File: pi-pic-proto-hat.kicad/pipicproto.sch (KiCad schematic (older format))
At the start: 20 parts, among them J1 RUN/~PGM~, J10 Conn_01x13_Male, J22 Conn_01x13_Male, J6 Barrel_Jack_Switch, J7 Conn_01x24_Male, J8 Conn_01x06_Male, J9 Conn_01x02_Male, P1 Conn_02x20_Odd_Even, Q1 IRF4905, U1 PIC12F675-IP

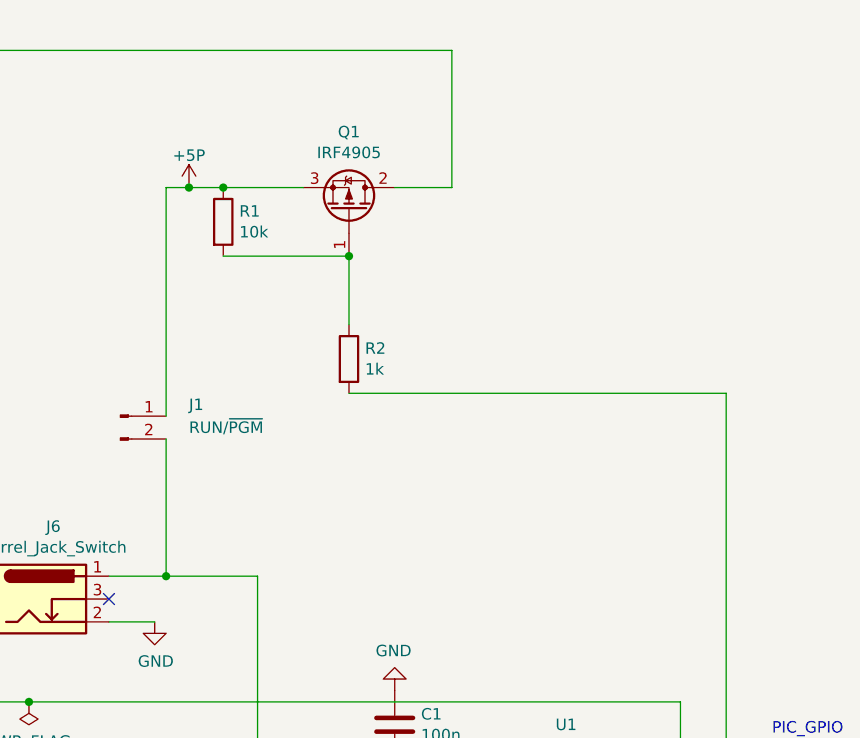
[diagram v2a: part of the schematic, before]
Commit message: V2.11: added LEDs
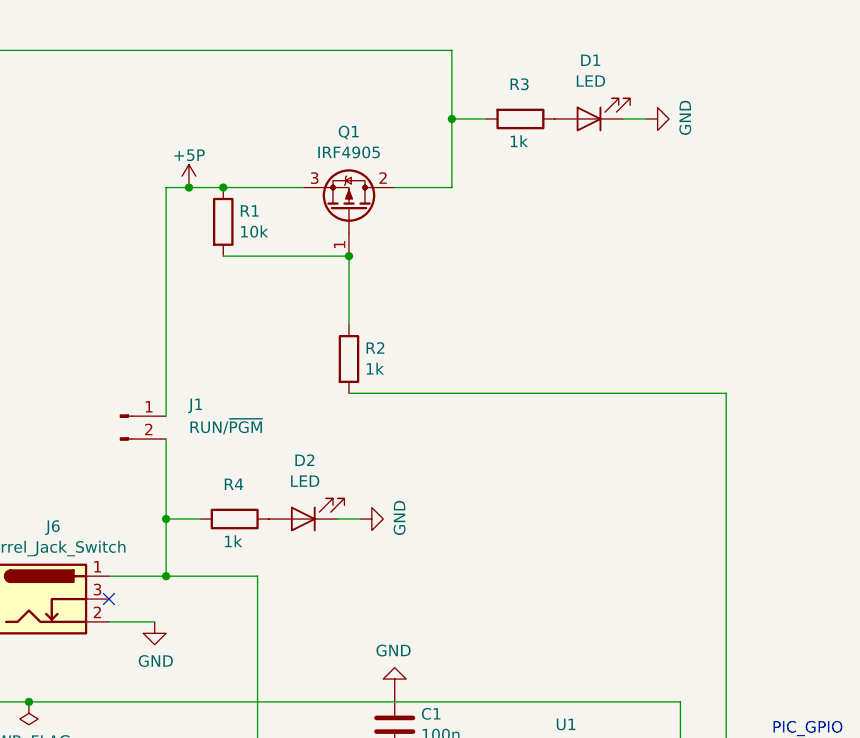
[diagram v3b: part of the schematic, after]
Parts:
- added D1, D2: LED, LED_SMD:LED_1206_3216Metric_Pad1.42x1.75mm_HandSolder, symbol Device:LED
- added R3, R4: 1k, Resistor_SMD:R_1206_3216Metric_Pad1.42x1.75mm_HandSolder, symbol Device:R
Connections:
- net +5V: now also R3.2
- net +5VP: now also R4.2
- net GND: now also D1.1 (K), D2.1 (K)
- new net: D1.2 (A), R3.1
- new net: D2.2 (A), R4.1
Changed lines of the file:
@@
 Sheet 1 1
 Title "PI PIC Prototyping Area"
-Date "2020-07-03"
-Rev "2.10"
+Date "2020-07-18"
+Rev "2.11"
 Comp "Bernhard Bablok, Lothar Hiller"
 Comment1 "https://github.com/bablokb/pi-pic-proto-hat"
@@
 Wire Wire Line
 	7500 1500 7750 1500
-Wire Wire Line
-	7750 900  7750 1500
 $Comp
 L Connector:Conn_01x13_Male J22
@@
 	6500 1500 6500 2500
 Wire Wire Line
-	6500 2600 6500 3200
+	6500 2600 6500 2950
 Connection ~ 6500 3200
 Wire Wire Line
@@
 Wire Wire Line
 	6900 3200 6900 4300
+$Comp
+L Device:R R3
+U 1 1 5F130E6C
+P 8050 1200
+F 0 "R3" V 7900 1150 50  0000 L CNN
+F 1 "1k" V 8150 1150 50  0000 L CNN
+F 2 "Resistor_SMD:R_1206_3216Metric_Pad1.42x1.75mm_HandSolder" V 7980 1200 50  0001 C CNN
+F 3 "~" H 8050 1200 50  0001 C CNN
+	1    8050 1200
+	0    1    1    0
+$EndComp
+$Comp
+L Device:LED D1
+U 1 1 5F137581
+P 8350 1200
+F 0 "D1" H 8343 945 50  0000 C CNN
+F 1 "LED" H 8343 1036 50  0000 C CNN
+F 2 "LED_SMD:LED_1206_3216Metric_Pad1.42x1.75mm_HandSolder" H 8350 1200 50  0001 C CNN
+F 3 "~" H 8350 1200 50  0001 C CNN
+	1    8350 1200
+	-1   0    0    1
+$EndComp
+$Comp
+L power:GND #PWR03
+U 1 1 5F14E188
+P 8600 1200
+F 0 "#PWR03" H 8600 950 50  0001 C CNN
+F 1 "GND" H 8605 1027 50  0000 C CNN
+F 2 "" H 8600 1200 50  0001 C CNN
+F 3 "" H 8600 1200 50  0001 C CNN
+	1    8600 1200
+	0    -1   -1   0
+$EndComp
+Wire Wire Line
+	7750 900  7750 1200
+Wire Wire Line
+	8500 1200 8600 1200
+Wire Wire Line
+	7900 1200 7750 1200
+Connection ~ 7750 1200
+Wire Wire Line
+	7750 1200 7750 1500
+$Comp
+L Device:R R4
+U 1 1 5F16FFEA
+P 6800 2950
+F 0 "R4" V 6650 2900 50  0000 L CNN
+F 1 "1k" V 6900 2900 50  0000 L CNN
+F 2 "Resistor_SMD:R_1206_3216Metric_Pad1.42x1.75mm_HandSolder" V 6730 2950 50  0001 C CNN
+F 3 "~" H 6800 2950 50  0001 C CNN
+	1    6800 2950
+	0    1    1    0
+$EndComp
+$Comp
+L Device:LED D2
+U 1 1 5F16FFF0
+P 7100 2950
+F 0 "D2" H 7093 2695 50  0000 C CNN
+F 1 "LED" H 7093 2786 50  0000 C CNN
+F 2 "LED_SMD:LED_1206_3216Metric_Pad1.42x1.75mm_HandSolder" H 7100 2950 50  0001 C CNN
+F 3 "~" H 7100 2950 50  0001 C CNN
+	1    7100 2950
+	-1   0    0    1
+$EndComp
+$Comp
+L power:GND #PWR04
+U 1 1 5F16FFF6
+P 7350 2950
+F 0 "#PWR04" H 7350 2700 50  0001 C CNN
+F 1 "GND" H 7355 2777 50  0000 C CNN
+F 2 "" H 7350 2950 50  0001 C CNN
+F 3 "" H 7350 2950 50  0001 C CNN
+	1    7350 2950
+	0    -1   -1   0
+$EndComp
+Wire Wire Line
+	7250 2950 7350 2950
+Wire Wire Line
+	6650 2950 6500 2950
+Connection ~ 6500 2950
+Wire Wire Line
+	6500 2950 6500 3200
 $EndSCHEMATC

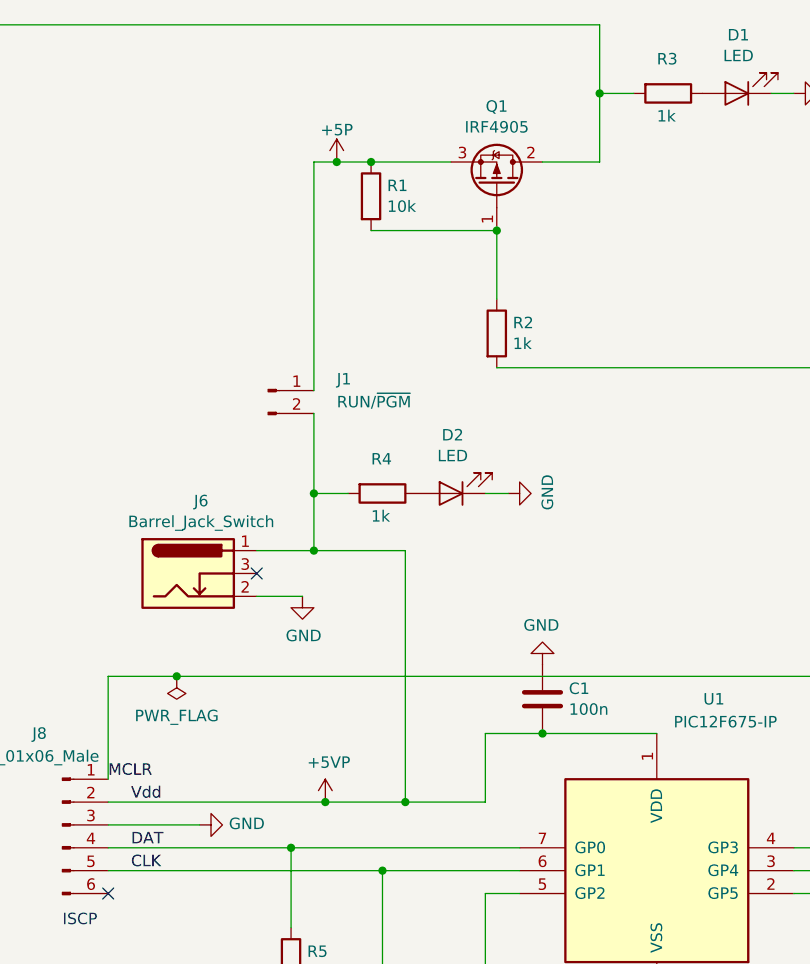
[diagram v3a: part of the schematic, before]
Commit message: V2.12: changed position of RUN-jumper
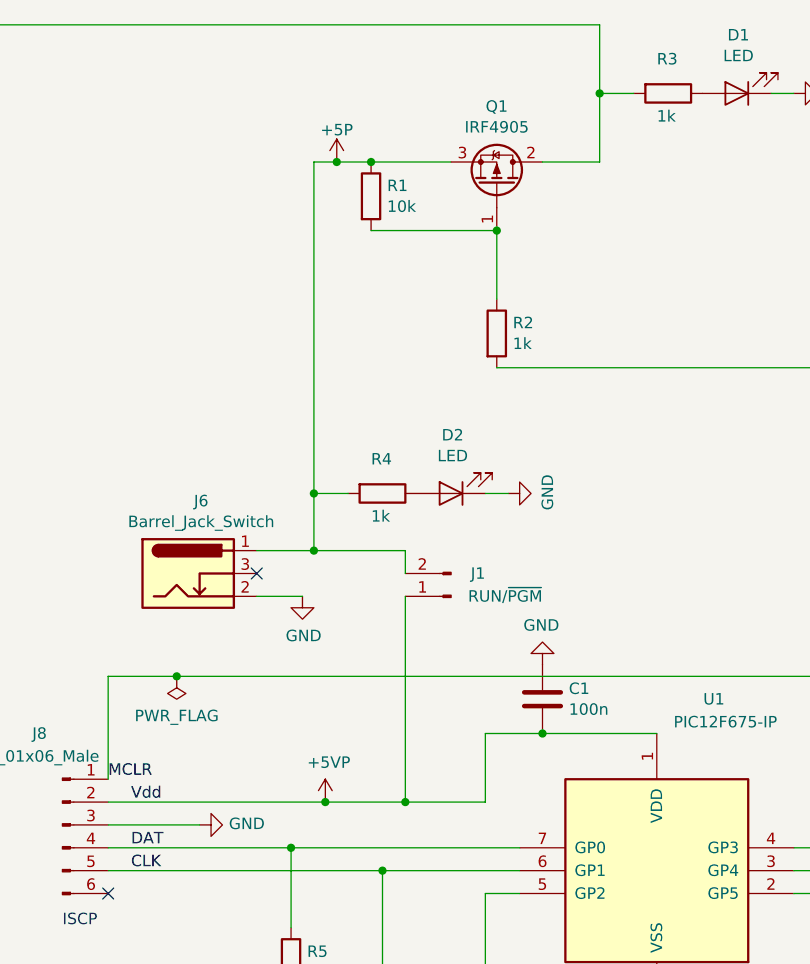
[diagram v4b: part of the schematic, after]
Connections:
- net +5P: now also J1.2 (Pin_2), J6.1, R4.2; no longer J1.1 (Pin_1)
- net +5VP: now also J1.1 (Pin_1); no longer J1.2 (Pin_2), J6.1, R4.2
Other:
- moved on the sheet: J1
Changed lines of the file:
@@
 Title "PI PIC Prototyping Area"
 Date "2020-07-18"
-Rev "2.11"
+Rev "2.12"
 Comp "Bernhard Bablok, Lothar Hiller"
 Comment1 "https://github.com/bablokb/pi-pic-proto-hat"
@@
 	1    0    0    -1
 $EndComp
-$Comp
-L Connector:Conn_01x02_Male J1
-U 1 1 5E41F5B6
-P 6300 2500
-F 0 "J1" H 6600 2550 50  0000 L CNN
-F 1 "RUN/~PGM~" H 6600 2450 50  0000 L CNN
-F 2 "Connector_PinHeader_2.54mm:PinHeader_1x02_P2.54mm_Vertical" H 6300 2500 50  0001 C CNN
-F 3 "~" H 6300 2500 50  0001 C CNN
-	1    6300 2500
-	1    0    0    -1
-$EndComp
 Wire Wire Line
 	3250 900  3250 1100
@@
 Wire Wire Line
 	6250 3200 6500 3200
-Wire Wire Line
-	6500 1500 6500 2500
-Wire Wire Line
-	6500 2600 6500 2950
 Connection ~ 6500 3200
-Wire Wire Line
-	6500 3200 6900 3200
 Wire Wire Line
 	6550 4300 6900 4300
@@
 	6900 4300 7250 4300
 Connection ~ 6900 4300
-Wire Wire Line
-	6900 3200 6900 4300
 $Comp
 L Device:R R3
@@
 Wire Wire Line
 	6500 2950 6500 3200
+$Comp
+L Connector:Conn_01x02_Male J1
+U 1 1 5E41F5B6
+P 7100 3400
+F 0 "J1" H 6950 3300 50  0000 L CNN
+F 1 "RUN/~PGM~" H 6700 3400 50  0000 L CNN
+F 2 "Connector_PinHeader_2.54mm:PinHeader_1x02_P2.54mm_Vertical" H 7100 3400 50  0001 C CNN
+F 3 "~" H 7100 3400 50  0001 C CNN
+	1    7100 3400
+	-1   0    0    1
+$EndComp
+Wire Wire Line
+	6900 3200 6900 3300
+Wire Wire Line
+	6900 3400 6900 4300
+Wire Wire Line
+	6500 1500 6500 2950
+Wire Wire Line
+	6500 3200 6900 3200
 $EndSCHEMATC

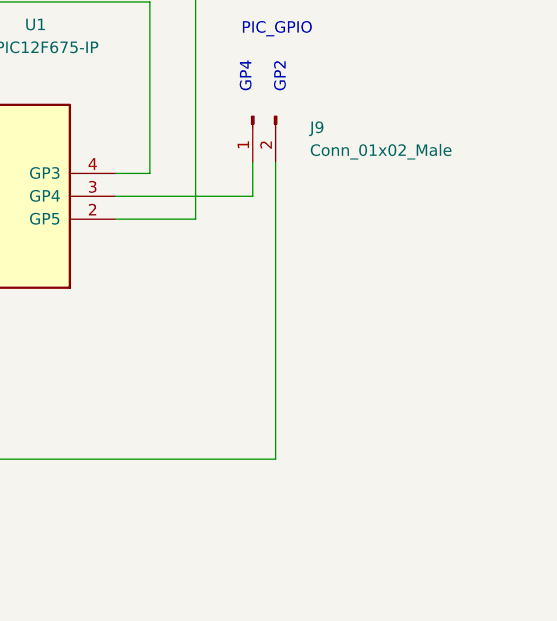
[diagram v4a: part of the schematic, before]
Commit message: V2.13: added button connected to GP2
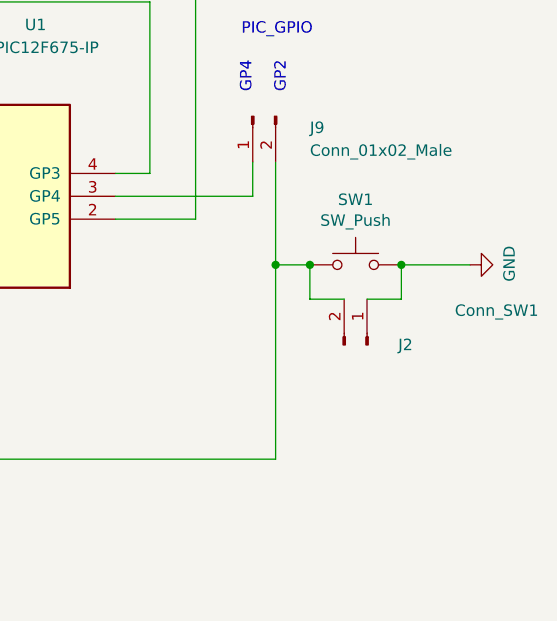
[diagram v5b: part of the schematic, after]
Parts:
- added J2: Conn_SW1, Connector_PinHeader_2.54mm:PinHeader_1x02_P2.54mm_Vertical, symbol Connector:Conn_01x02_Male
- added SW1: SW_Push, user:SW_PUSH_SLIM_1x4, symbol Switch:SW_Push
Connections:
- net GND: now also J2.1 (Pin_1), SW1.2
- net at J9.2 (Pin_2), U1.5 (GP2): now also J2.2 (Pin_2), SW1.1
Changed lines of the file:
@@
 Sheet 1 1
 Title "PI PIC Prototyping Area"
-Date "2020-07-18"
-Rev "2.12"
+Date "2020-07-23"
+Rev "2.13"
 Comp "Bernhard Bablok, Lothar Hiller"
 Comment1 "https://github.com/bablokb/pi-pic-proto-hat"
@@
 	7250 5750 9300 5750
 Wire Wire Line
-	9300 5750 9300 4450
+	9300 5750 9300 4900
 Text Notes 9200 4150 1    50   ~ 0
 GP4
@@
 Wire Wire Line
 	6500 3200 6900 3200
+$Comp
+L Switch:SW_Push SW1
+U 1 1 5F19E2FA
+P 9650 4900
+F 0 "SW1" H 9650 5185 50  0000 C CNN
+F 1 "SW_Push" H 9650 5094 50  0000 C CNN
+F 2 "user:SW_PUSH_SLIM_1x4" H 9650 5100 50  0001 C CNN
+F 3 "~" H 9650 5100 50  0001 C CNN
+	1    9650 4900
+	1    0    0    -1
+$EndComp
+Wire Wire Line
+	9450 4900 9300 4900
+Connection ~ 9300 4900
+Wire Wire Line
+	9300 4900 9300 4450
+$Comp
+L power:GND #PWR05
+U 1 1 5F1A4F9E
+P 10150 4900
+F 0 "#PWR05" H 10150 4650 50  0001 C CNN
+F 1 "GND" H 10155 4727 50  0000 C CNN
+F 2 "" H 10150 4900 50  0001 C CNN
+F 3 "" H 10150 4900 50  0001 C CNN
+	1    10150 4900
+	0    -1   -1   0
+$EndComp
+Wire Wire Line
+	9850 4900 10150 4900
+$Comp
+L Connector:Conn_01x02_Male J2
+U 1 1 5F1ABA22
+P 9700 5250
+F 0 "J2" V 9700 5450 50  0000 R CNN
+F 1 "Conn_SW1" V 9850 6000 50  0000 R CNN
+F 2 "Connector_PinHeader_2.54mm:PinHeader_1x02_P2.54mm_Vertical" H 9700 5250 50  0001 C CNN
+F 3 "~" H 9700 5250 50  0001 C CNN
+	1    9700 5250
+	0    1    -1   0
+$EndComp
+Wire Wire Line
+	9850 4900 9850 5050
+Wire Wire Line
+	9850 5050 9700 5050
+Connection ~ 9850 4900
+Wire Wire Line
+	9450 4900 9450 5050
+Wire Wire Line
+	9450 5050 9600 5050
+Connection ~ 9450 4900
 $EndSCHEMATC

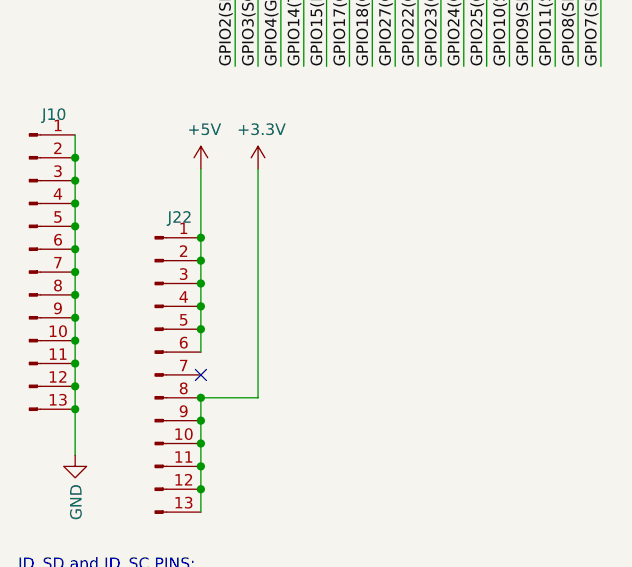
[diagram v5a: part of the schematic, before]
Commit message: V2.14: removed dead button from power connector
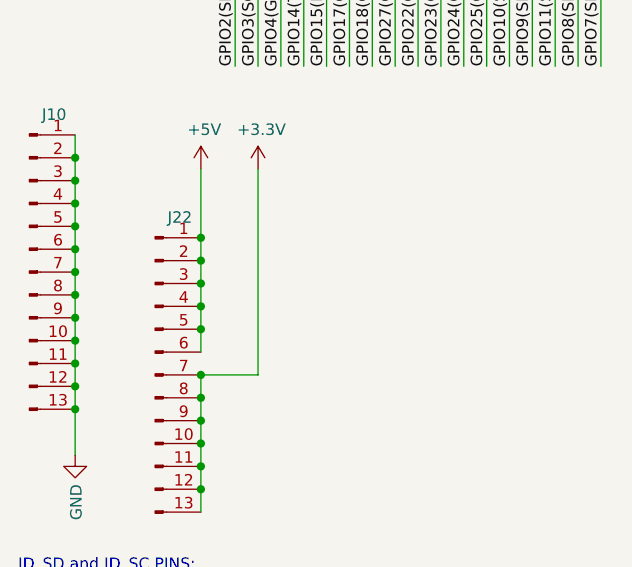
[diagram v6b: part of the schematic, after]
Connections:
- net +3V3: now also J22.7 (Pin_7)
- no-connect marks 5 -> 4
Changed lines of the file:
@@
 Sheet 1 1
 Title "PI PIC Prototyping Area"
-Date "2020-07-23"
-Rev "2.13"
+Date "2020-07-24"
+Rev "2.14"
 Comp "Bernhard Bablok, Lothar Hiller"
 Comment1 "https://github.com/bablokb/pi-pic-proto-hat"
@@
 Wire Wire Line
 	1450 5650 1450 5750
-NoConn ~ 1450 5850
 $Comp
 L power:+3.3V #PWR0101
@@
 	1450 6350 1450 6250
 Wire Wire Line
-	1700 4950 1700 5950
-Wire Wire Line
-	1700 5950 1450 5950
-Connection ~ 1450 5950
+	1700 4950 1700 5850
 Wire Wire Line
 	8600 4700 8950 4700
@@
 	9450 5050 9600 5050
 Connection ~ 9450 4900
+Wire Wire Line
+	1450 5950 1450 5850
+Connection ~ 1450 5950
+Wire Wire Line
+	1450 5850 1700 5850
+Connection ~ 1450 5850
 $EndSCHEMATC

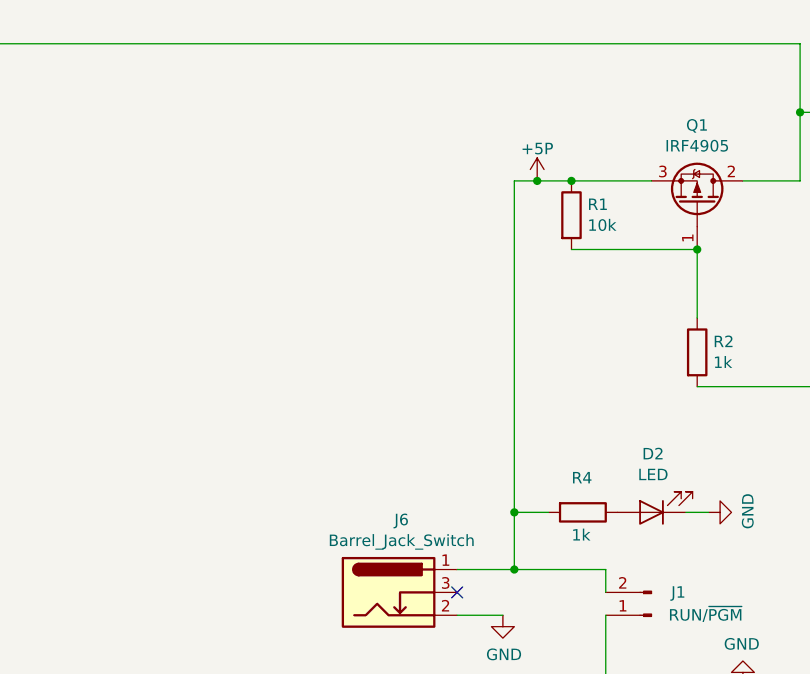
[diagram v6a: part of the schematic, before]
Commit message: V2.15: added connector for +5P (5V permanently on)
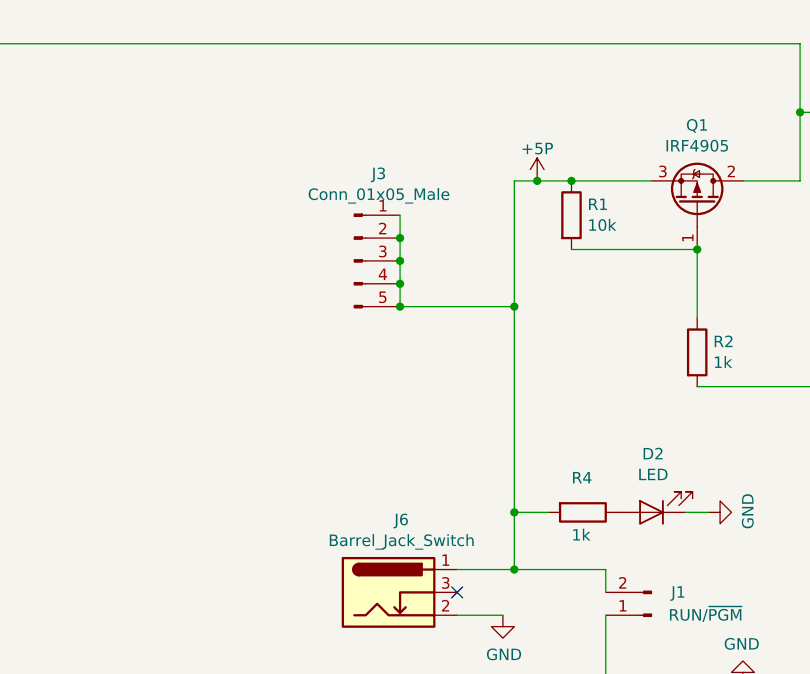
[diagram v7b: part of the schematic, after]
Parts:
- added J3: Conn_01x05_Male, Connector_PinHeader_2.54mm:PinHeader_1x05_P2.54mm_Vertical, symbol Connector:Conn_01x05_Male
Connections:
- net +5P: now also J3.1 (Pin_1), J3.2 (Pin_2), J3.3 (Pin_3), J3.4 (Pin_4), J3.5 (Pin_5)
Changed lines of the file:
@@
 Title "PI PIC Prototyping Area"
 Date "2020-07-24"
-Rev "2.14"
+Rev "2.15"
 Comp "Bernhard Bablok, Lothar Hiller"
 Comment1 "https://github.com/bablokb/pi-pic-proto-hat"
@@
 	6900 3400 6900 4300
 Wire Wire Line
-	6500 1500 6500 2950
+	6500 1500 6500 2050
 Wire Wire Line
 	6500 3200 6900 3200
@@
 	1450 5850 1700 5850
 Connection ~ 1450 5850
+$Comp
+L Connector:Conn_01x05_Male J3
+U 1 1 5F1C34FF
+P 5800 1850
+F 0 "J3" H 5908 2231 50  0000 C CNN
+F 1 "Conn_01x05_Male" H 5908 2140 50  0000 C CNN
+F 2 "Connector_PinHeader_2.54mm:PinHeader_1x05_P2.54mm_Vertical" H 5800 1850 50  0001 C CNN
+F 3 "~" H 5800 1850 50  0001 C CNN
+	1    5800 1850
+	1    0    0    -1
+$EndComp
+Wire Wire Line
+	6500 2050 6000 2050
+Wire Wire Line
+	6000 2050 6000 1950
+Connection ~ 6500 2050
+Wire Wire Line
+	6500 2050 6500 2950
+Connection ~ 6000 2050
+Wire Wire Line
+	6000 1850 6000 1750
+Wire Wire Line
+	6000 1950 6000 1850
+Connection ~ 6000 1950
+Connection ~ 6000 1850
+Wire Wire Line
+	6000 1750 6000 1650
+Connection ~ 6000 1750
 $EndSCHEMATC
